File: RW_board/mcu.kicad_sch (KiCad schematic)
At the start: 0 parts

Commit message: Completed MCU schematic, connected with driver schematic
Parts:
- added C10, C9: 20n, Capacitor_SMD:C_0402_1005Metric, symbol Device:C
- added C11: 4.7n, Capacitor_SMD:C_0402_1005Metric, symbol Device:C
- added C12, C15, C16, C17, C18: 100n, Capacitor_SMD:C_0402_1005Metric, symbol Device:C
- added C13: 1u, Capacitor_SMD:C_0402_1005Metric, symbol Device:C
- added C14: 4.7u, Capacitor_SMD:C_0402_1005Metric, symbol Device:C
- added D4: PRTR5V0U2X,215, PRTR5V0U2X, symbol RW_Imports:PRTR5V0U2X,215
- added D5: LED, symbol Device:LED
- added J1: USB4105-GF-A, USB4105-GF-A:GCT_USB4105-GF-A, symbol RW_Imports:USB4105-GF-A
- added J2: 20021521-00010T4LF, 2002152100010T4LF, symbol RW_Imports:20021521-00010T4LF
- added R11: 1M, Resistor_SMD:R_0402_1005Metric, symbol Device:R
- added R12: 39R, Resistor_SMD:R_0402_1005Metric, symbol Device:R
- added R13: 330R, Resistor_SMD:R_0402_1005Metric, symbol Device:R
- added R14: 10k, Resistor_SMD:R_0402_1005Metric, symbol Device:R
- added R15: 1k, Resistor_SMD:R_0402_1005Metric, symbol Device:R
- added R16: 330, symbol Device:R
- added R17, R18: 5.1k, Resistor_SMD:R_0402_1005Metric, symbol Device:R
- added SW1: SW_Push, symbol Switch:SW_Push
- added U1: ATSAMD21G18A-M, Package_DFN_QFN:QFN-48-1EP_7x7mm_P0.5mm_EP5.15x5.15mm, symbol MCU_Microchip_SAMD:ATSAMD21G18A-M
- added Y1: 32.768KHz, 830105946101, symbol RW_Imports:830105946101
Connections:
- new net: C9.2, U1.1 (PA00), Y1.
- new net: C10.2, U1.2 (PA01), Y1.2 (CRYSTAL_2)
- new net: J2.10, R12.1
- new net: J1.B5 (CC2), R17.1
- new net: C13.2, U1.43 (VDDCORE)
- new net: C12.2, R13.2, R14.1, SW1.2
- new net: J1.A5 (CC1), R18.1
- new net: D5.2 (A), R16.2
- new net: R16.1, U1.7 (PB08)
- new net +3.3V: C14.2, C15.2, C16.2, C17.2, C18.2, J2.1, R14.2, R15.2, U1.17 (VDDIO), U1.36 (VDDIO), U1.44 (VDDIN), U1.6 (VDDANA)
- new net CS: U1.30 (PA21)
- new net D_N: D4.3 (input/output_2), J1.A7 (DN1), J1.B7 (DN2), U1.33 (PA24)
- new net D_P: D4.2 (input/output_1), J1.A6 (DP1), J1.B6 (DP2), U1.34 (PA25)
- new net GND: C10.1, C11.2, C12.1, C13.1, C14.1, C15.1, C16.1, C17.1, C18.1, C9.1, D5.1 (K), J1.A1_B12 (GND), J1.B1_A12 (GND), J2.3, J2.5, R11.2, R13.1, R17.2, R18.2, U1.18 (GND), U1.35 (GND), U1.42 (GND), U1.49 (EP), U1.5 (GNDANA)
- new net MCU_nRESET: R12.2, SW1.1, U1.40 (~{RESET})
- new net MISO: U1.28 (PA19)
- new net MOSI: U1.25 (PA16)
- new net MOTOR_BRAKE: U1.15 (PA10)
- new net MOTOR_DIR: U1.32 (PA23)
- new net MOTOR_DRVOFF: U1.16 (PA11)
- new net MOTOR_SPEED: U1.29 (PA20)
- new net MOTOR_nSLEEP: U1.19 (PB10)
- new net Motor_PWM: U1.31 (PA22)
- new net Motor_nFAULT: U1.20 (PB11)
- new net SCK: U1.26 (PA17)
- new net SHIELD: C11.1, D4.1 (ground), J1.SH1 (SHELL_GND), J1.SH2 (SHELL_GND), J1.SH3 (SHELL_GND), J1.SH4 (SHELL_GND), R11.1
- new net SWCLK: J2.4, R15.1, U1.45 (PA30)
- new net SWDIO: J2.2, U1.46 (PA31)
- new net VBUS: D4.4 (supply_voltage), J1.A4_B9 (VBUS), J1.B4_A9 (VBUS)

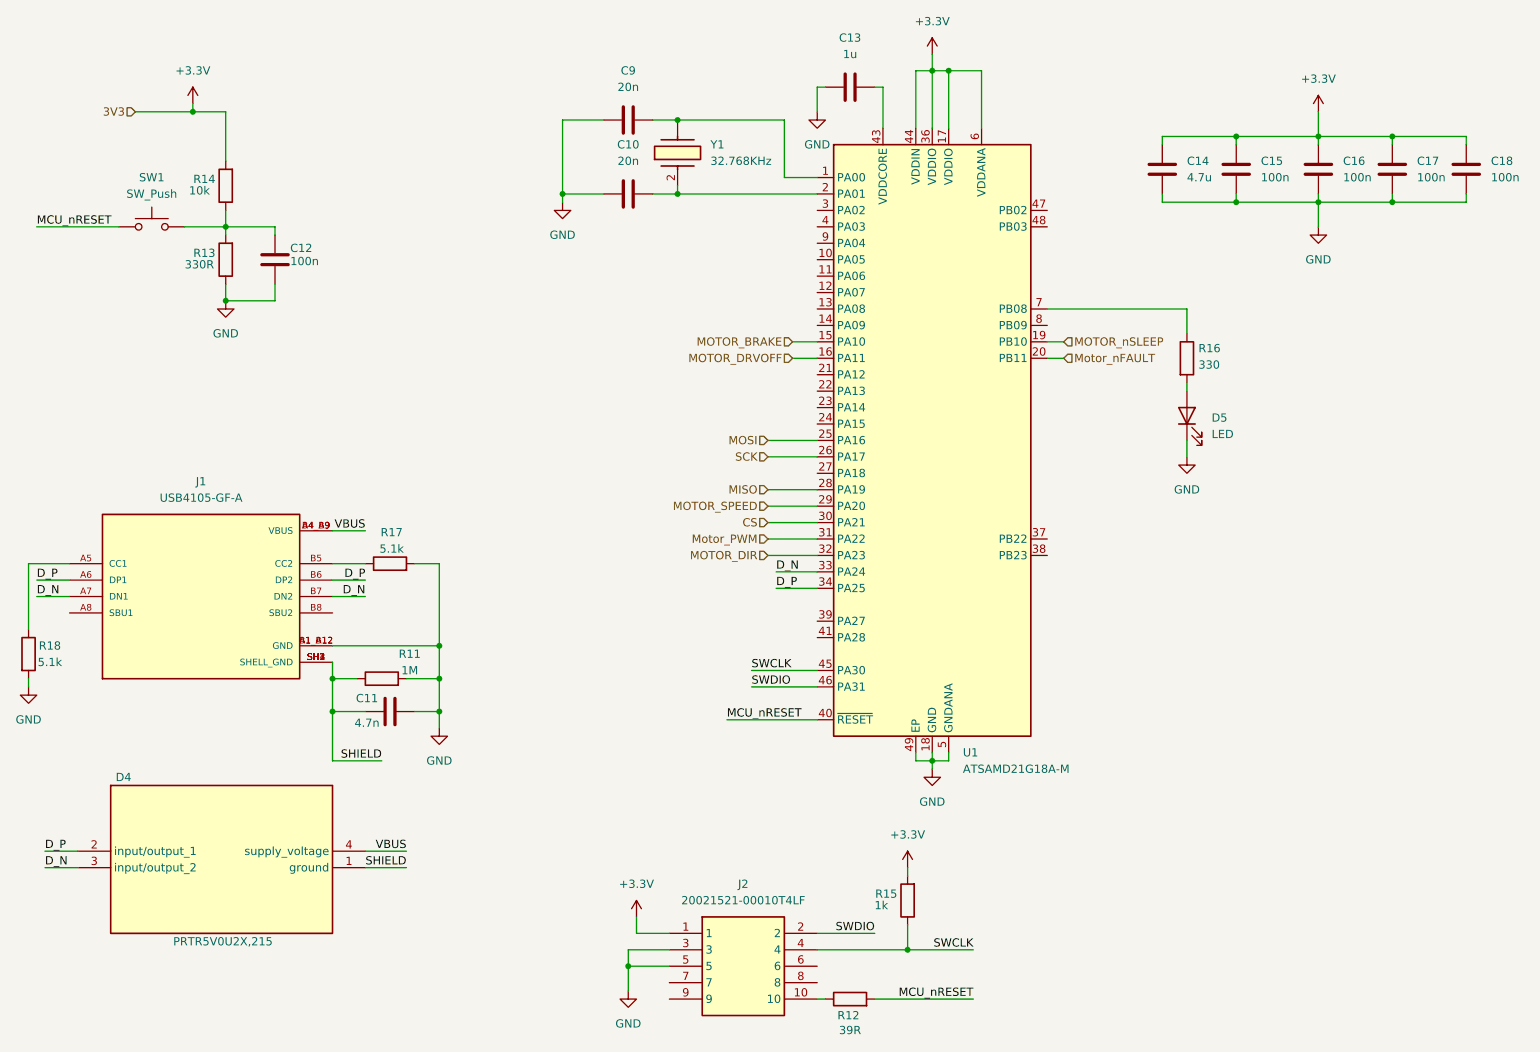
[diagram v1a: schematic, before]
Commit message: Switched motor, added connectors, finished up design
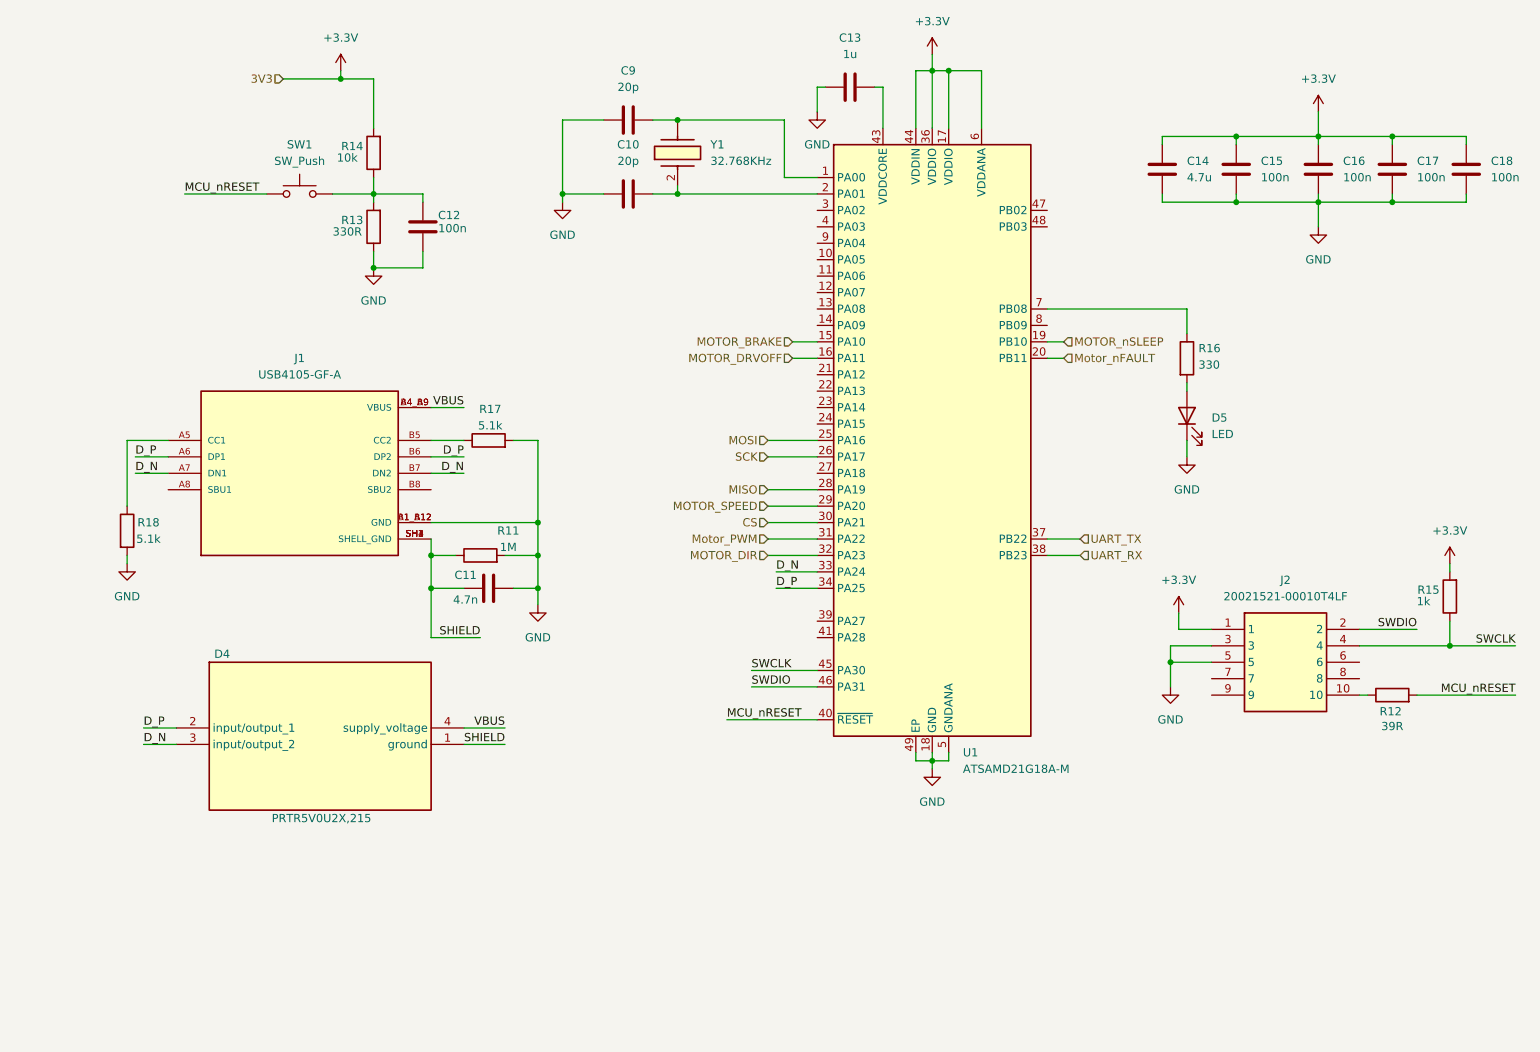
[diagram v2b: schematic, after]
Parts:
- C10, C9: value 20n -> 20p
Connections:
- net UART_TX: now reaches U1.37 (PB22)
- net UART_RX: now reaches U1.38 (PB23)
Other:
- moved on the sheet: C11, C12, D4, J1, J2, R11, R12, R13, R14, R15, R17, R18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

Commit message: Fixed reset switch
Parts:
- D5: value LED -> YELLOW
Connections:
- net MCU_nRESET: now also C12.2, R14.1
- net at R13.2, SW1.2: no longer C12.2, R14.1

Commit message: Added ADC inputs
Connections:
- net DAC0: now reaches U1.3 (PA02)
- net ADC1: now reaches U1.47 (PB02)
- net ADC2: now reaches U1.48 (PB03)
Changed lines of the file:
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@@
+	(wire
+		(pts
+			(xy 142.24 48.26) (xy 146.05 48.26)
+		)
+		(stroke
+			(width 0)
+			(type default)
+		)
+	)
 	(wire
 		(pts
@@
 	(wire
 		(pts
+			(xy 181.61 48.26) (xy 184.15 48.26)
+		)
+		(stroke
+			(width 0)
+			(type default)
+		)
+	)
+	(wire
+		(pts
 			(xy 40.64 88.9) (xy 45.72 88.9)
 		)
@@
 		(pts
 			(xy 223.52 27.94) (xy 223.52 30.48)
+		)
+		(stroke
+			(width 0)
+			(type default)
+		)
+	)
+	(wire
+		(pts
+			(xy 181.61 50.8) (xy 184.15 50.8)
 		)
 		(stroke
@@
 		)
 	)
+	(hierarchical_label "ADC2"
+		(shape input)
+		(at 184.15 50.8 0)
+		(effects
+			(font
+				(size 1.27 1.27)
+			)
+			(justify left)
+		)
+	)
+	(hierarchical_label "ADC1"
+		(shape input)
+		(at 184.15 48.26 0)
+		(effects
+			(font
+				(size 1.27 1.27)
+			)
+			(justify left)
+		)
+	)
 	(hierarchical_label "MOTOR_DIR"
 		(shape input)
@@
 		(effects
 			(font
+				(size 1.27 1.27)
+			)
+			(justify right)
+		)
+	)
+	(hierarchical_label "DAC0"
+		(shape output)
+		(at 142.24 48.26 180)
+		(effects
+			(font
